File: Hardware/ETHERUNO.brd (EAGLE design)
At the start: 68.6 x 53.3 mm, 98 parts, among them IC1 MC33269DT-5.0, IC2 CP2102N-A01-GQFN24, IC4 LM358D, IC5 ATMEGA328P TQFP32, IC6 W6100-LQFP, IC7 MCP24AA025E48, J1 DC_2_1MM, J2 USB-C-16P-16P, P2 ICSP:MAIN, P4 microSD, Q1 FDN340P, Q2 2N7002, U1 HY931147C-RJ45

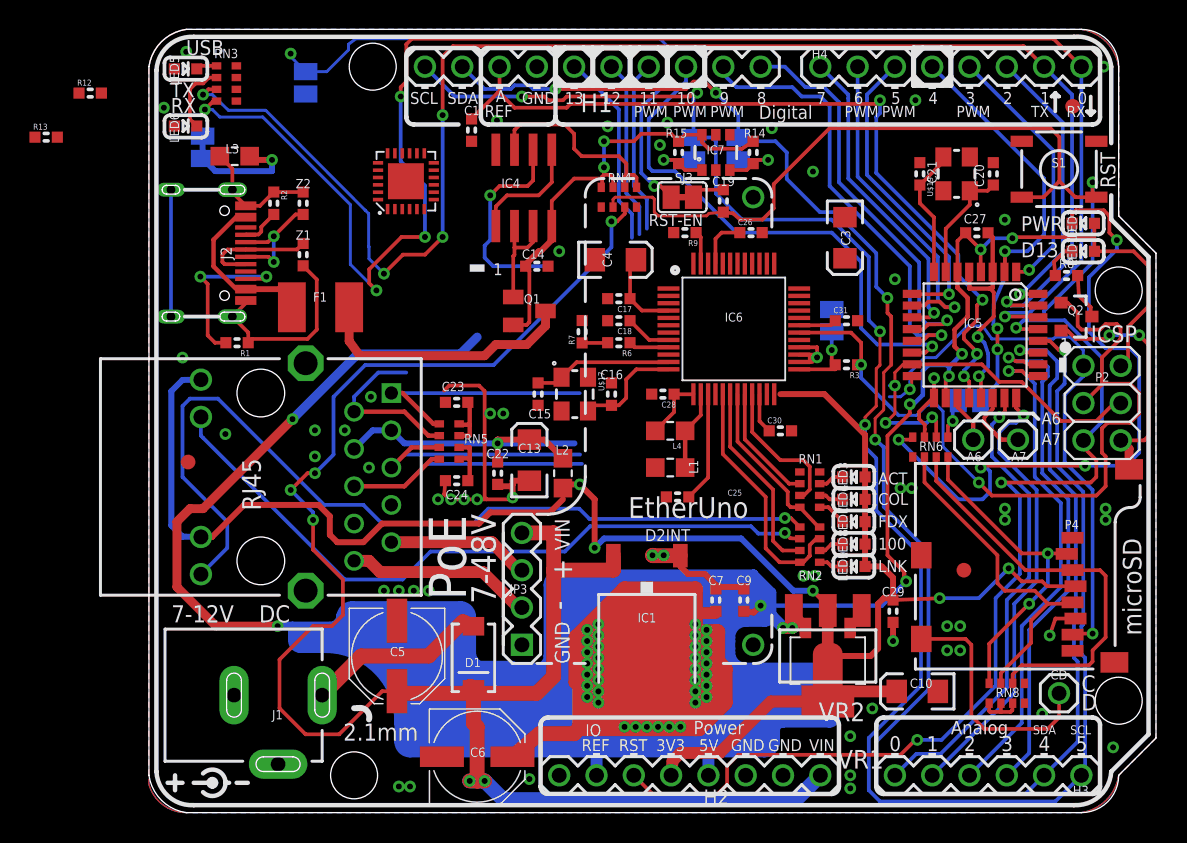
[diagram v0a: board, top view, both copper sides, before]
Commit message: Final routing and DRC for v4.0 release
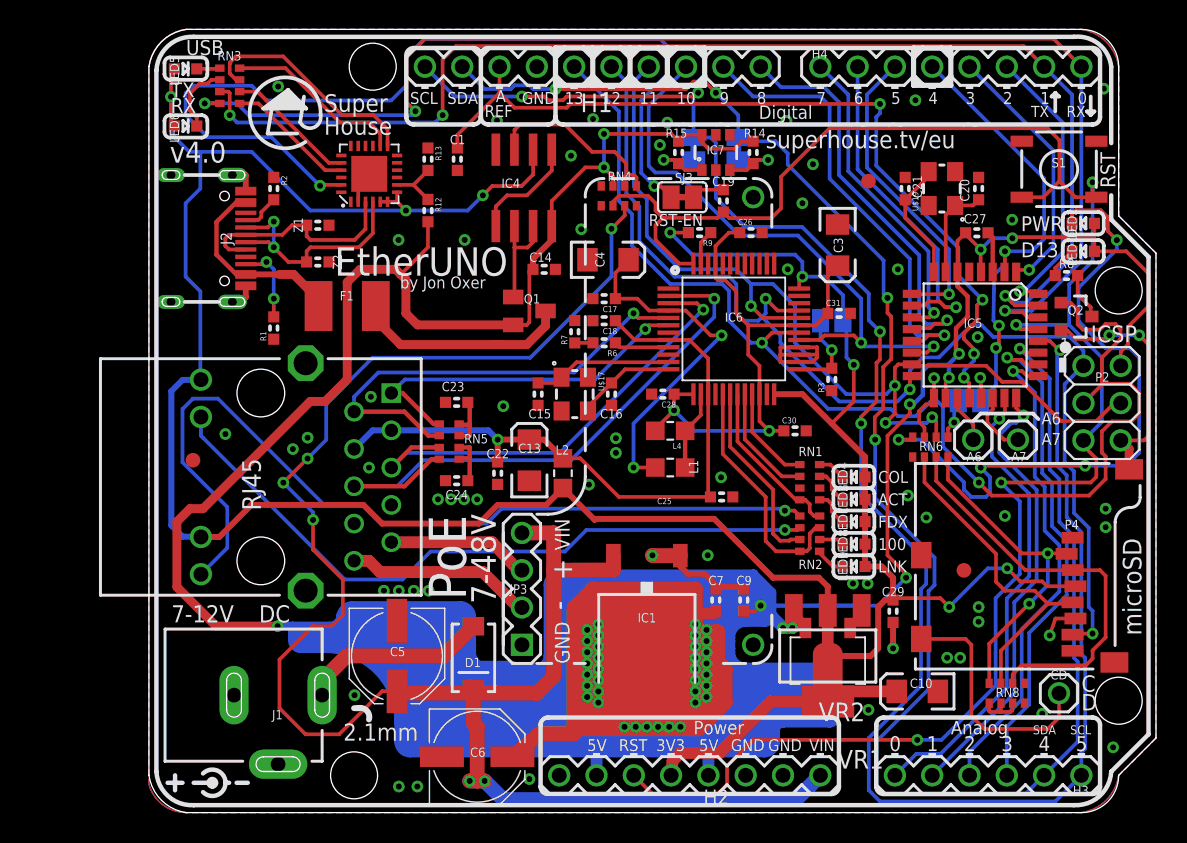
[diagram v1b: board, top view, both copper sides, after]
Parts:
- removed L3: 0805 INDUCTOR, SuperHouse-DiscreteSemi:0805-LARGE
- removed SJ1: GROUND, SuperHouse-Jumpers:SJC
- removed SJ2: UBOOT, SuperHouse-Jumpers:SJ
- SJ4: value (none) -> MODE
- moved R13 26.0 mm to (19.0, 44.5), turned to 270 degrees
- moved R12 24.4 mm to (19.0, 41.0), turned to 270 degrees
- moved FID1 14.8 mm to (49.0, 43.0)
- moved Z2 4.12 mm to (11.5, 37.5), turned to 0 degrees
- moved C25 3.00 mm to (39.0, 21.5), turned to 0 degrees
- moved R1 2.69 mm to (8.50, 33.0), turned to 90 degrees
- moved IC2 2.55 mm to (15.0, 43.5)
- moved Z1 2.24 mm to (11.5, 40.0), turned to 0 degrees
- moved C1 2.21 mm to (21.0, 44.5)
- moved F1 1.82 mm to (13.5, 34.5)
- moved LED3 1.52 mm to (48.0, 21.3)
- moved LED4 1.52 mm to (48.0, 22.9)
- moved C20 1.41 mm to (56.5, 42.5)
- moved C21 1.41 mm to (51.5, 42.5)
- moved R3 1.41 mm to (46.5, 29.5), turned to 90 degrees
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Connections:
- removed net N$328: LED4.C, RN1.6
- removed net N$9: J2.A12B1, J2.A1B12, J2.FIX1, J2.FIX2, J2.FIX3, J2.FIX4, L3.1, R1.1, R2.1, Z1.2, Z2.2
- removed net USBGND: L3.2, SJ1.1
- new net N$8: LED4.C, RN1.8
- net COLLED: now also RN1.1; no longer RN1.3
- net DTR: no longer SJ2.2
- net GND: now also J2.A12B1, J2.A1B12, J2.FIX1, J2.FIX2, J2.FIX3, J2.FIX4, R1.1, R2.1, Z1.2, Z2.2; no longer SJ1.2, SJ2.1
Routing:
- net 3.3V: track 143.7 -> 211.9 mm, vias 6 -> 8
- net N$9: track 38.9 -> 0.00 mm
- net D11_MOSI: track 38.5 -> 66.9 mm, vias 3 -> 4
- net D12_MISO: track 52.0 -> 79.8 mm, vias 2 -> 3
- net 5V: track 1175.3 -> 1201.5 mm, vias 49 -> 48
- net 1V2D: track 13.2 -> 38.1 mm, vias 0 -> 2
- net DTR: track 39.7 -> 62.7 mm
- net D0_RX: track 109.7 -> 89.3 mm, vias 5 -> 3
- net RXIN: track 11.7 -> 31.4 mm, vias 0 -> 1
- net GND: track 73.0 -> 53.6 mm
- net 1V2A: track 5.77 -> 24.3 mm, vias 0 -> 2
- net TXON: track 22.7 -> 40.3 mm, vias 0 -> 1
- net D1_TX: track 101.3 -> 85.1 mm, vias 5 -> 3
- net RX_LED: track 0.03 -> 15.7 mm
- net D13_SCK: track 73.4 -> 88.7 mm
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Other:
- board text added: "D4/CS"
- board text added: "EtherUNO"
- board text added: "SKU: EU"
- board text added: "Super House"
- board text added: "Wiznet Mode Open: W6100 Closed: W5500"
- board text added: "by Jon Oxer"
- board text added: "superhouse.tv/eu"
- board text added: "~"
- board text removed: "D2INT"
- board text removed: "EtherUno"
- board text removed: "IO"
- board text removed: "PWM"
- board text removed: "SKU: ET"
- board text removed: "UBOOT"
- board text removed: "by Jonathan Oxer"

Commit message: Major rework for W5500, ready for v1.0 release
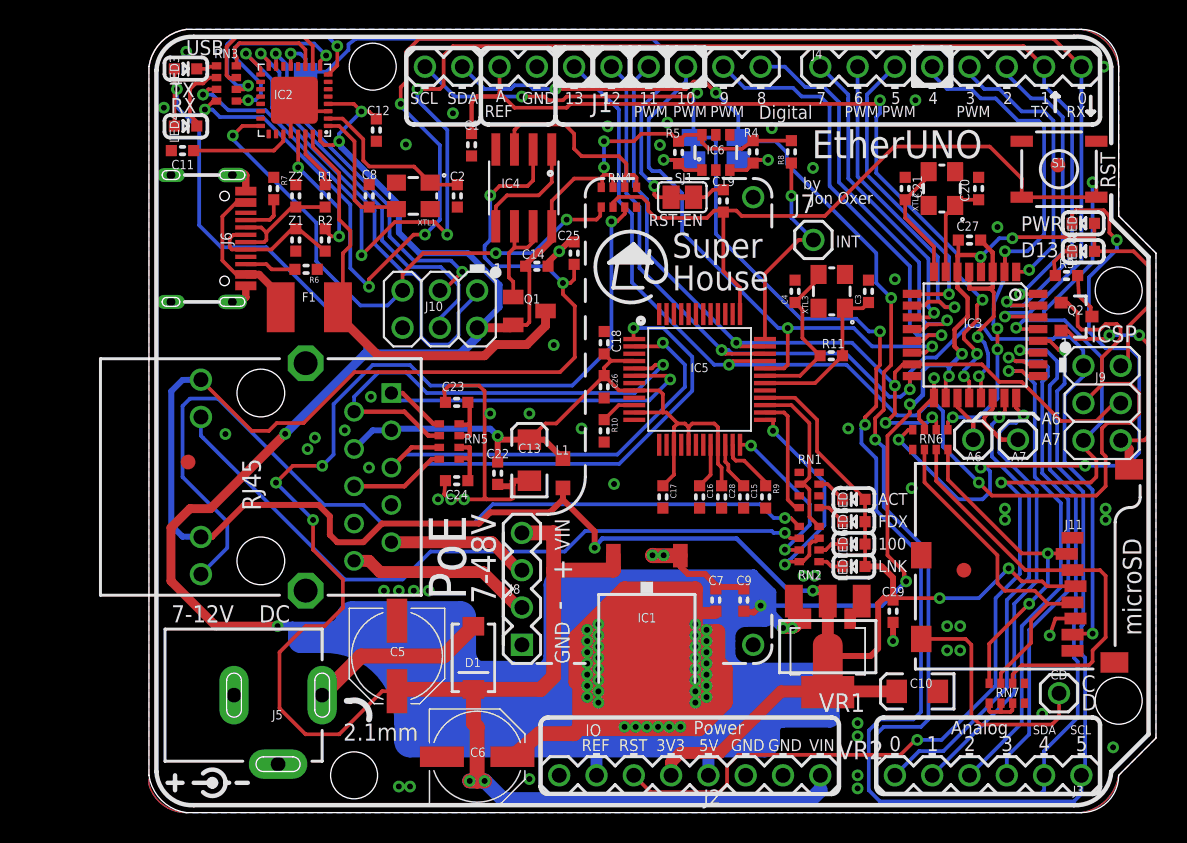
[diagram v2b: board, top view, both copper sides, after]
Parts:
- removed C30, C31: 100nF, SuperHouse-DiscreteSemi:C0603
- removed H1: Digital_8_13, SuperHouse-Connectors:1X10-S
- removed H2: Power, SuperHouse-Connectors:1X08-S
- removed IC7: MCP24AA025E48, freetronics-jon:SOT23-6
- removed L2, L4: 1uH 250mA 0805, SuperHouse-DiscreteSemi:0805-LARGE
- removed LED10: D13/RED, SuperHouse-LEDs:LED-0603
- removed LED9: YELLOW, SuperHouse-LEDs:LED-0603
- removed R12: 22.1K, SuperHouse-DiscreteSemi:R0603
- removed R13: 47.5K, SuperHouse-DiscreteSemi:R0603
- removed R14: 4K7, SuperHouse-DiscreteSemi:R0603
- removed SJ5, SJ6, SJ7: SJC, SuperHouse-Jumpers:SJC
- removed U$17: CRYSTAL-GND3X2, SuperHouse-Oscillators:CRYSTAL-SMD-3X2
- added C11: 1uF 0603, SuperHouse-DiscreteSemi:C0603
- added C12: 100nF 0603, SuperHouse-DiscreteSemi:C0603
- added C2, C8: 22pF 0603, SuperHouse-DiscreteSemi:C0603
- added IC3: ATMEGA328P TQFP32, SuperHouse-MCUs:TQFP32-08
- added J10: ICSP:USB, SuperHouse-Connectors:2X03-ICSP
- added J5: DC_2_1MM, SuperHouse-Connectors:POWER_JACK_SLOTS
- added J6: USB-C-16P-16P, SuperHouse-Connectors:USB-C-16P
- added J7: INT, SuperHouse-Connectors:1X01
- added LED1: PWR/BLUE, SuperHouse-LEDs:LED-0603
- added R10: 12.4K 1%, SuperHouse-DiscreteSemi:R0603
- added R11: 1M, SuperHouse-DiscreteSemi:R0603
- added R4: 4K7, SuperHouse-DiscreteSemi:R0603
- added SJ1: RESET-EN, SuperHouse-Jumpers:SJC
- added SJ2: UBOOT, SuperHouse-Jumpers:SJ
- added XTL1: 16MHz, SuperHouse-Oscillators:CRYSTAL-SMD-3X2
- added XTL3: 25MHz, SuperHouse-Oscillators:CRYSTAL-SMD-3X2
- A6: value M01 -> A6
- A7: value M01 -> A7
- C14, C29: value 100nF 0603 -> 100nF
- C15: value 13pF -> 10nF
- C16: value 13pF -> 4.7uF
- C18: value 100nF -> 10nF
- C20, C21: value 22pF 0603 -> 15pF
- C3, C4: value 10uF 6.3V A TANT -> 18pF; device SuperHouse-DiscreteSemi:EIA3216 -> SuperHouse-DiscreteSemi:C0603
- C5, C6: device SuperHouse-DiscreteSemi:PANASONIC_D -> rcl:PANASONIC_D
- CD: value M01 -> M01-PLAIN
- IC2: value CP2102N-A01-GQFN24 -> ATMEGA16U2-MU; device SuperHouse-ICs:QFN-24 -> SuperHouse-MCUs:ATMEL_QFN32
- IC4: device linear:SO08 -> SuperHouse-ICs:SO08
- IC5: value ATMEGA328P TQFP32 -> W5500-LQFP; device SuperHouse-MCUs:TQFP32-08 -> SuperHouse-ICs:LQFP48
- IC6: value W6100-LQFP -> MCP24AA025E48; device SuperHouse-ICs:LQFP48 -> freetronics-jon:SOT23-6
- J1: value DC_2_1MM -> Digital_8_13; device SuperHouse-Connectors:POWER_JACK_SLOTS -> SuperHouse-Connectors:1X10-S
- J2: value USB-C-16P-16P -> Power; device SuperHouse-Connectors:USB-C-16P -> SuperHouse-Connectors:1X08-S
- L1: device SuperHouse-DiscreteSemi:0805-LARGE -> rcl:L2012C
- LED2: value PWR/BLUE -> YELLOW
- LED3: value YELLOW -> TX/YEL
- LED4: value RED -> RX/GRN
- LED5: value TX/YEL -> GREEN
- LED6: value RX/GRN -> GREEN
- LED7: value GREEN -> YELLOW
- LED8: value GREEN -> D13/RED
- R1, R2: value 5K1 -> 22R
- R3: value 10K -> 1K
- R6: value 12K 1% -> 5K1
- R7: value 300R 1% -> 5K1
- R8: value 1K 0603 -> 10K
- RN1, RN2: value 330R -> 1K
- SJ3: value RESET-EN -> SJC-NORMAL
- SJ4: value MODE -> SJC-NORMAL; device SuperHouse-Jumpers:SJ -> SuperHouse-Jumpers:SJC
- VR1: value LD1117-SOT223 -> LD1117-SOT89; device SuperHouse-Regulators:SOT-223 -> SuperHouse-Regulators:SOT89
- VR2: value LD1117-SOT89 -> LD1117-SOT223; device SuperHouse-Regulators:SOT89 -> SuperHouse-Regulators:SOT-223
- XTL2: value CRYSTAL-GND3X2 -> 16MHz
- moved LED5 55.0 mm to (48.0, 19.8), turned to 180 degrees
- moved LED3 54.1 mm to (2.50, 50.7), turned to 0 degrees
- moved LED6 53.7 mm to (48.0, 18.3), turned to 180 degrees
- moved J1 53.5 mm to (30.2, 50.8), turned to 180 degrees
- moved LED4 51.4 mm to (2.50, 46.8), turned to 0 degrees
- moved J2 50.8 mm to (36.8, 2.54), turned to 0 degrees
- moved LED8 25.3 mm to (63.6, 38.2)
- moved LED2 24.4 mm to (48.0, 21.3)
- moved R7 22.7 mm to (8.50, 42.5), turned to 270 degrees
- moved R6 20.9 mm to (10.7, 37.0)
- moved R8 20.5 mm to (43.8, 45.0), turned to 90 degrees
- moved C25 19.4 mm to (29.0, 38.1), turned to 90 degrees
- moved IC5 19.0 mm to (37.5, 29.5), turned to 0 degrees
- moved R9 18.6 mm to (42.0, 21.5), turned to 270 degrees
- moved R3 17.5 mm to (62.5, 36.6), turned to 180 degrees
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- renumbered H3 to J3, H4 to J4, JP3 to J8, P2 to J9, P4 to J11, R15 to R5, RN8 to RN7, U$19 to XTL2
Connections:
- removed net 1V2A: C17.1, C4.A, IC6.4, L1.2
- removed net 1V2D: C26.1, C28.1, C3.A, C30.1, C31.1, IC6.13, IC6.22, IC6.31, IC6.45, L4.2
- removed net COLLED: IC6.21, RN1.1
- removed net D+: IC2.3, J2.A6, J2.B6, Z1.1
- removed net D-: IC2.4, J2.A7, J2.B7, Z2.1
- removed net D11_MOSI: H1.4, IC5.15, IC6.32, J9.4, RN6.6
- removed net D12_MISO: H1.5, IC5.16, IC6.33, J11.7, J9.1
- removed net MODE: IC6.25, R3.2, SJ4.1
- removed net N$32: C16.1, IC6.12, U$17.3
- removed net N$36: IC6.9, R6.1
- removed net N$37: IC6.47, R9.1
- removed net N$39: IC2.8, R12.1, R13.2
- removed net RX_LED: IC2.13, RN3.7
- removed net TX_LED: IC2.14, RN3.8
- new net CIPO2: IC2.17, J10.1
- new net COPI2: IC2.16, J10.4
- new net D11_COPI: IC3.15, IC5.35, J1.4, J9.4, RN6.6
- new net D12_CIPO: IC3.16, IC5.34, J1.5, J11.7, J9.1
- new net N$113: C2.2, IC2.2, XTL1.1
- new net N$117: C11.1, IC2.27
- new net N$16: J6.A6, J6.B6, R2.2, Z1.1
- new net N$17: J6.A7, J6.B7, R1.2, Z2.1
- new net N$31: C16.1, IC5.20
- new net N$33: IC5.10, R10.1
- new net N$9: J6.B5, R6.2
- new net RD+: IC2.29, R2.1
- new net RD-: IC2.30, R1.1
- new net RESET2: IC2.24, J10.5, RN4.1
- new net RXLED: IC2.10, RN3.7
- new net SCK2: IC2.15, J10.3
- new net TXLED: IC2.11, RN3.8
- net 1V2O: now also C15.1, IC5.22; no longer IC6.14, L1.1, L4.1
- net 3.3V: now also C25.1, IC5.28, J2.4, L1.1, LED2.A; no longer H2.4, IC2.5, IC2.6, IC2.7, IC6.24, IC6.36, L2.1, LED3.A, LED4.A, LED8.A, LED9.A, R9.2, SJ4.2
- net 3V3A: now also C17.1, C26.1, C28.1, IC5.11, IC5.15, IC5.17, IC5.21, IC5.4, IC5.8, L1.2; no longer C25.1, IC6.15, IC6.8, L2.2
- net 5V: now also C12.1, IC2.32, IC2.4, IC3.18, IC3.4, IC3.6, IC6.6, J10.2, J2.2, J2.5, LED1.A, LED3.A, LED4.A, LED8.A, R4.1, R8.2, RN4.8; no longer H2.2, H2.5, IC5.18, IC5.4, IC5.6, IC7.6, LED10.A, LED2.A, R12.2, R14.1
- net A0: now also IC3.23; no longer IC5.23
- net A1: now also IC3.24; no longer IC5.24
- net A2: now also IC3.25; no longer IC5.25
- net A3: now also IC3.26; no longer IC5.26
- net A4_SDA: now also IC3.27, J1.9, SJ3.1; no longer H1.9, IC5.27, SJ5.1
- net A5_SCL: now also IC3.28, J1.10, SJ4.1; no longer H1.10, IC5.28, SJ6.1
- net ACTLED: now also IC5.27, RN2.8; no longer IC6.20
- net AREF: now also IC3.20, J1.8; no longer H1.8, IC5.20
- net D0_RX: now also IC3.30; no longer IC5.30
- net D10_CS: now also IC3.14, IC5.32, J1.3; no longer H1.3, IC5.14, IC6.29
- net D13_SCK: now also IC3.17, IC5.33, J1.6; no longer H1.6, IC5.17, IC6.30
- net D1_TX: now also IC3.31; no longer IC5.31
- net D2: now also IC3.32; no longer IC5.32
- net D3: now also IC3.1; no longer IC5.1
- net D4: now also IC3.2, RN6.5; no longer IC5.2, SJ7.2
- net D5: now also IC3.9; no longer IC5.9
- net D6: now also IC3.10; no longer IC5.10
- net D7: now also IC3.11; no longer IC5.11
- net D8: now also IC3.12, J1.1; no longer H1.1, IC5.12
- net D9: now also IC3.13, J1.2; no longer H1.2, IC5.13
- net DTR: now also IC2.13, SJ1.1, SJ2.2; no longer IC2.23, SJ3.1
- net FDXLED: now also IC5.26; no longer IC6.19, RN2.8
- net GND: now also C11.2, C12.2, C2.1, C3.2, C4.2, C8.1, IC2.28, IC2.3, IC2.EXP, IC3.21, IC3.3, IC3.5, IC5.14, IC5.16, IC5.19, IC5.29, IC5.48, IC5.9, IC6.2, IC6.4, IC6.5, J1.7, J10.6, J2.6, J2.7, J5.GND, J5.GNDBREAK, J6.A12B1, J6.A1B12, J6.FIX1, J6.FIX2, J6.FIX3, J6.FIX4, R10.2, R6.1, R7.1, R9.2, SJ2.1, XTL1.2, XTL1.4, XTL3.2, XTL3.4; no longer C3.C, C30.2, C31.2, C4.C, H1.7, H2.6, H2.7, IC2.2, IC2.TGND, IC5.21, IC5.5, IC6.1, IC6.10, IC6.16, IC6.23, IC6.26, IC6.27, IC6.28, IC6.46, IC6.7, IC7.2, IC7.4, IC7.5, J1.GND, J1.GNDBREAK, J2.A12B1, J2.A1B12, J2.FIX1, J2.FIX2, J2.FIX3, J2.FIX4, R1.1, R13.1, R2.1, R3.1, R7.2, U$17.2, U$17.4
- net LINKLED: now also IC5.25; no longer IC6.17
- net N$10: now also C4.1, IC5.31, R11.1, XTL3.3; no longer J2.B5, R1.2
- net N$11: now also LED4.C; no longer LED6.C
- net N$115: now also J6.A4B9, J6.A9B4; no longer J2.A4B9, J2.A9B4
- net N$13: now also LED3.C; no longer LED5.C
- net N$14: now also LED1.C; no longer LED2.C
- net N$2: now also IC3.7; no longer IC5.7
- net N$21: now also IC3.22; no longer IC5.22
- net N$22: now also IC3.19; no longer IC5.19
- net N$26: now also LED6.C; no longer LED8.C
- net N$27: now also C3.1, IC5.30, R11.2, XTL3.1; no longer RN6.5, SJ7.1
- net N$28: now also LED7.C; no longer LED9.C
- net N$29: now also IC6.3, R4.2, SJ3.2; no longer IC7.3, R14.2, SJ5.2
- net N$3: now also SJ1.2; no longer SJ3.2
- net N$30: now also J6.A5, R7.2; no longer C15.1, IC6.11, U$17.1
- net N$327: now also LED5.C; no longer LED7.C
- net N$329: now also LED2.C; no longer LED3.C
- net N$34: now also IC5.23, R9.1; no longer J2.A5, R2.2
- net N$35: now also IC5.36, J7.1, R8.1; no longer R6.2, R7.1
- net N$4: now also LED8.C, R3.2; no longer LED10.C, R8.2
- net N$5: now also IC6.1, SJ4.2; no longer IC7.1, SJ6.2
- net N$6: now also R3.1; no longer R8.1
- net N$60: now also J5.PWR; no longer J1.PWR
- net N$7: now also IC3.8; no longer IC5.8
- net N$8: now also C8.2, IC2.1, XTL1.3; no longer LED4.C, RN1.8
- net RESET: now also IC3.29, IC5.37, J2.3; no longer H2.3, IC5.29, IC6.48
- net RXIN: now also IC5.5; no longer IC6.5
- net RXIP: now also IC5.6; no longer IC6.6
- net SPDLED: now also IC5.24; no longer IC6.18
- net TXON: now also IC5.1; no longer IC6.2
- net TXOP: now also IC5.2; no longer IC6.3
- net USBRXD: now also IC2.9; no longer IC2.21
- net USBTXD: now also IC2.8; no longer IC2.20
- net USBVCC: now also IC2.31
- net VIN: now also J2.8; no longer H2.8
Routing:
- net D12_MISO: track 79.8 -> 0.00 mm, vias 3 -> 0
- net D12_CIPO: track 0.00 -> 78.0 mm, vias 0 -> 3
- net D11_MOSI: track 66.9 -> 0.00 mm, vias 4 -> 0
- net D11_COPI: track 0.00 -> 61.9 mm, vias 0 -> 4
- net 1V2D: track 38.1 -> 0.00 mm, vias 2 -> 0
- net RESET2: track 0.00 -> 37.5 mm, vias 0 -> 3
- net 5V: track 1201.5 -> 1236.5 mm, vias 48 -> 52
- net CIPO2: track 0.00 -> 33.0 mm, vias 0 -> 1
- net COPI2: track 0.00 -> 27.1 mm, vias 0 -> 1
- net GND: track 53.6 -> 78.7 mm
- net SCK2: track 0.00 -> 24.5 mm, vias 0 -> 2
- net 1V2A: track 24.3 -> 0.00 mm, vias 2 -> 0
- net DTR: track 62.7 -> 41.0 mm
- net D0_RX: track 89.3 -> 108.9 mm, vias 3 -> 5
- net D1_TX: track 85.1 -> 103.8 mm, vias 3 -> 5
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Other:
- board text added: "Copyright 2020 SuperHouse Automation P/L Released under the TAPR Open Hardware License tapr.org/OHL"
- board text added: "INT"
- board text added: "IO"
- board text added: "Jon Oxer"
- board text added: "PWM"
- board text added: "UBOOT"
- board text added: "by"
- board text removed: "CC"
- board text removed: "COL"
- board text removed: "D4/CS"
- board text removed: "Wiznet Mode Open: W6100 Closed: W5500"
- board text removed: "by Jon Oxer"
- board text removed: "superhouse.tv/eu"
- board text removed: "v4.0"
- board text removed: "~"

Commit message: Fix Ethernet data line bias resistors. Add strong pullups and pulldowns to mode and RSVD pins. Improve silkscreen. Add diode to PoE VIN to protect against backpower.
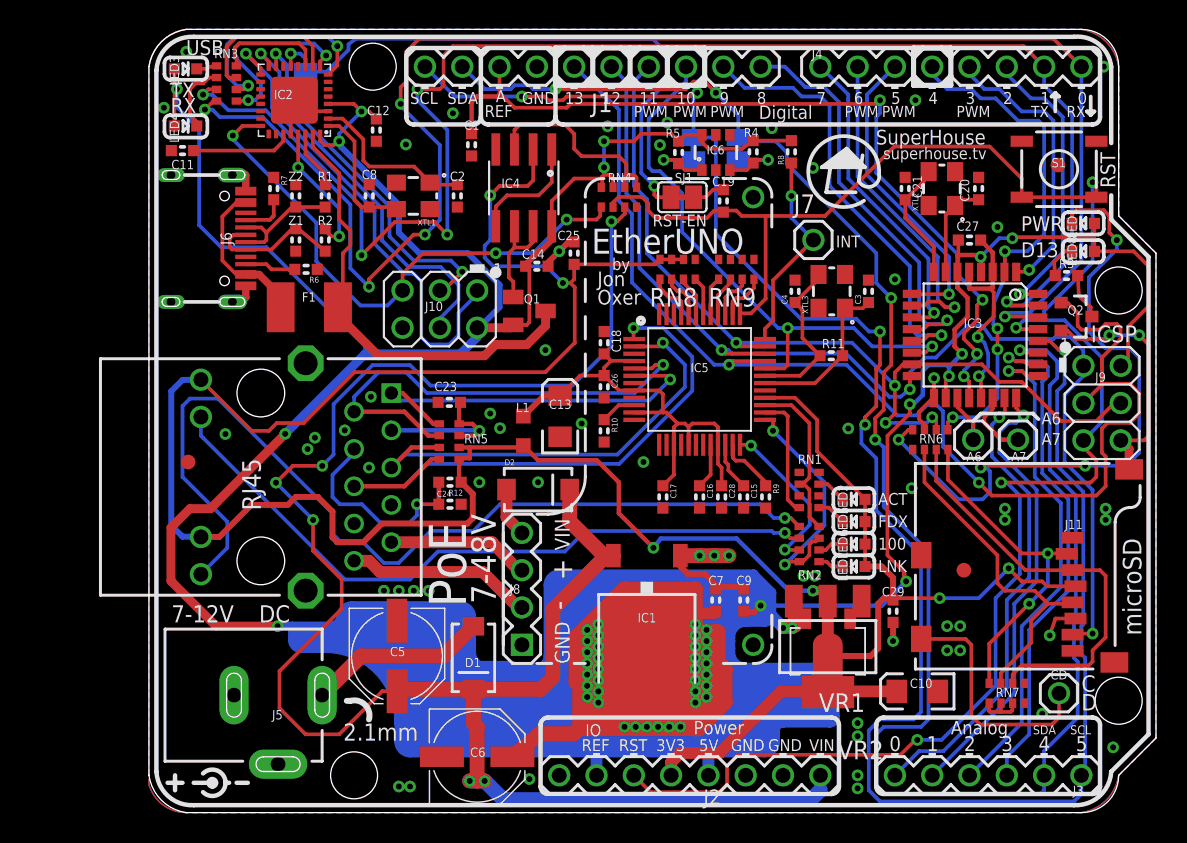
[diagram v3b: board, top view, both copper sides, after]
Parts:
- removed C22: 100nF, SuperHouse-DiscreteSemi:C0603
- added D2: 1N4004, SuperHouse-DiscreteSemi:SMA-DIODE
- added R12: 10R, SuperHouse-DiscreteSemi:R0603
- added RN8, RN9: 10K, SuperHouse-DiscreteSemi:CAY16
- C23: value 100nF -> 10nF
- C24: value 100nF -> 22nF
- D1: value 1N4004 SMB -> 1N4004
- moved L1 3.95 mm to (25.5, 26.0)
- moved C13 3.65 mm to (28.0, 27.0)
- moved C24 1.67 mm to (20.5, 21.0), turned to 0 degrees
- moved C23 0.50 mm to (20.5, 27.9)
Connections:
- removed net N$321: C23.1, RN5.7, RN5.8
- new net N$15: D2.A, J8.4
- new net N$32: C24.1, R12.2, U1.P$4
- new net N$36: IC5.45, RN8.1
- new net N$37: IC5.44, RN8.2
- new net N$38: IC5.43, RN8.3
- new net N$39: IC5.42, RN8.4
- new net N$40: IC5.41, RN9.1
- new net N$41: IC5.40, RN9.2
- new net N$42: IC5.39, RN9.3
- new net N$43: IC5.38, RN9.4
- net 3.3V: now also R12.1, RN5.5, RN5.6, RN8.6, RN8.7, RN8.8
- net 3V3A: no longer C22.1, U1.P$3, U1.P$4
- net GND: now also RN8.5, RN9.5, RN9.6, RN9.7, RN9.8; no longer C22.2
- net N$1: now also C23.1, RN5.7, RN5.8, U1.P$3; no longer C24.1, RN5.5, RN5.6
- net VIN: now also D2.C; no longer J8.4
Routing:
- net GND: track 78.7 -> 59.7 mm
- net 3V3A: track 51.0 -> 33.0 mm, vias 1 -> 0
- net 3.3V: track 194.4 -> 209.7 mm
- net N$32: track 0.00 -> 14.3 mm, vias 0 -> 1
- net N$1: track 3.90 -> 10.6 mm, vias 0 -> 1
- net N$321: track 3.90 -> 0.00 mm
- net N$15: track 0.00 -> 3.38 mm
- net N$43: track 0.00 -> 3.29 mm
- net N$36: track 0.00 -> 3.29 mm
- net N$42: track 0.00 -> 3.15 mm
- net N$37: track 0.00 -> 3.05 mm
- net N$67: track 60.4 -> 63.4 mm
- net N$41: track 0.00 -> 2.73 mm
- net N$38: track 0.00 -> 2.73 mm
- net N$40: track 0.00 -> 2.60 mm
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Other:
- board text added: "SuperHouse"
- board text added: "superhouse.tv"
- board text added: "v1.1"
